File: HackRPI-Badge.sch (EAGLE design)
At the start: 42 parts, among them J1 FTDI_BASICPTH, J2 SOLDERJUMPERTRACE-PTH, U2 3.3V, U4 74595, U5 74595, U6 74595, U7 74165DT, U8 AT25FS010

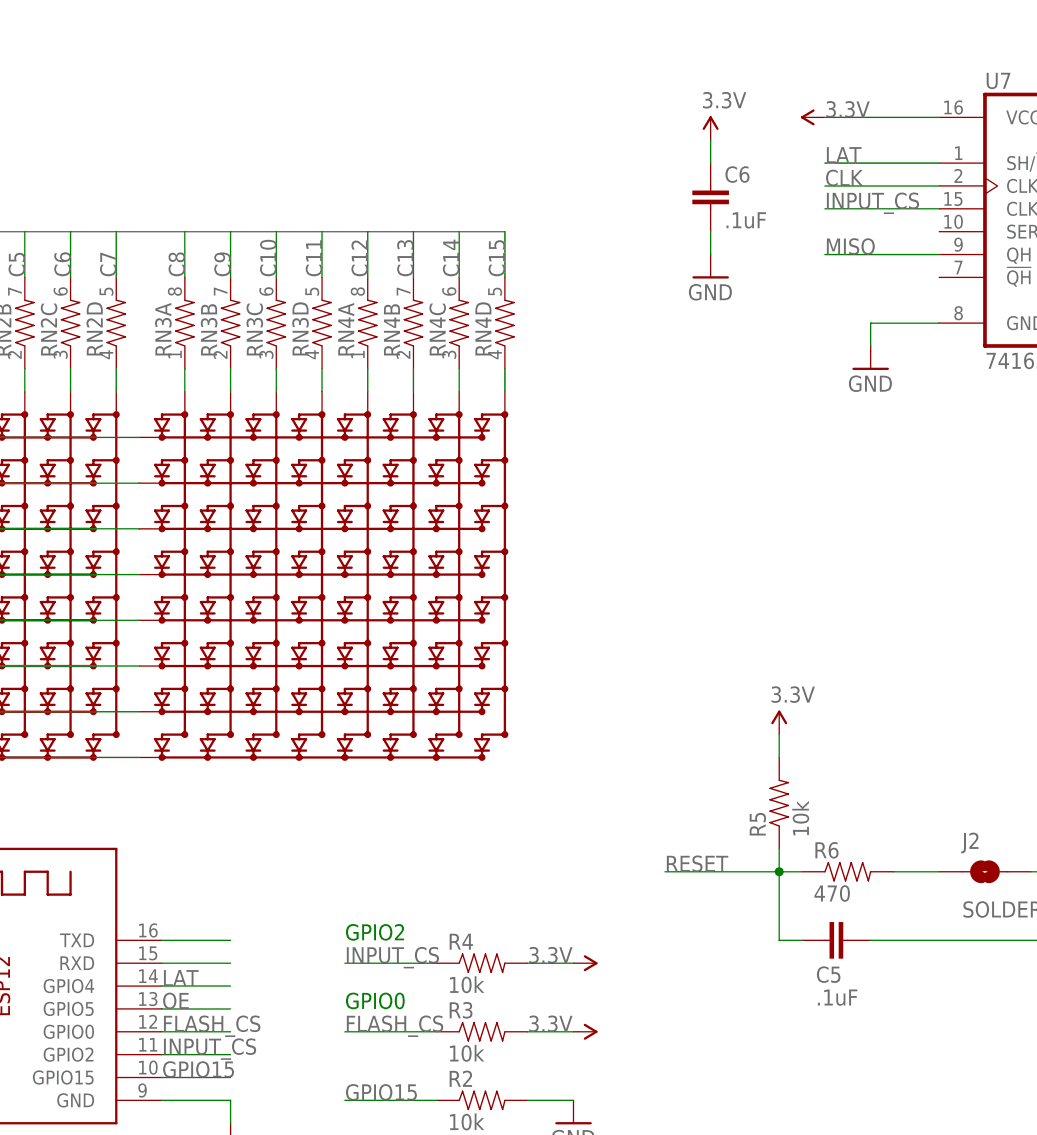
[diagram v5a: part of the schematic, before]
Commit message: Fixed 74165 sck pin connection, updated gitignore to ignore lock files
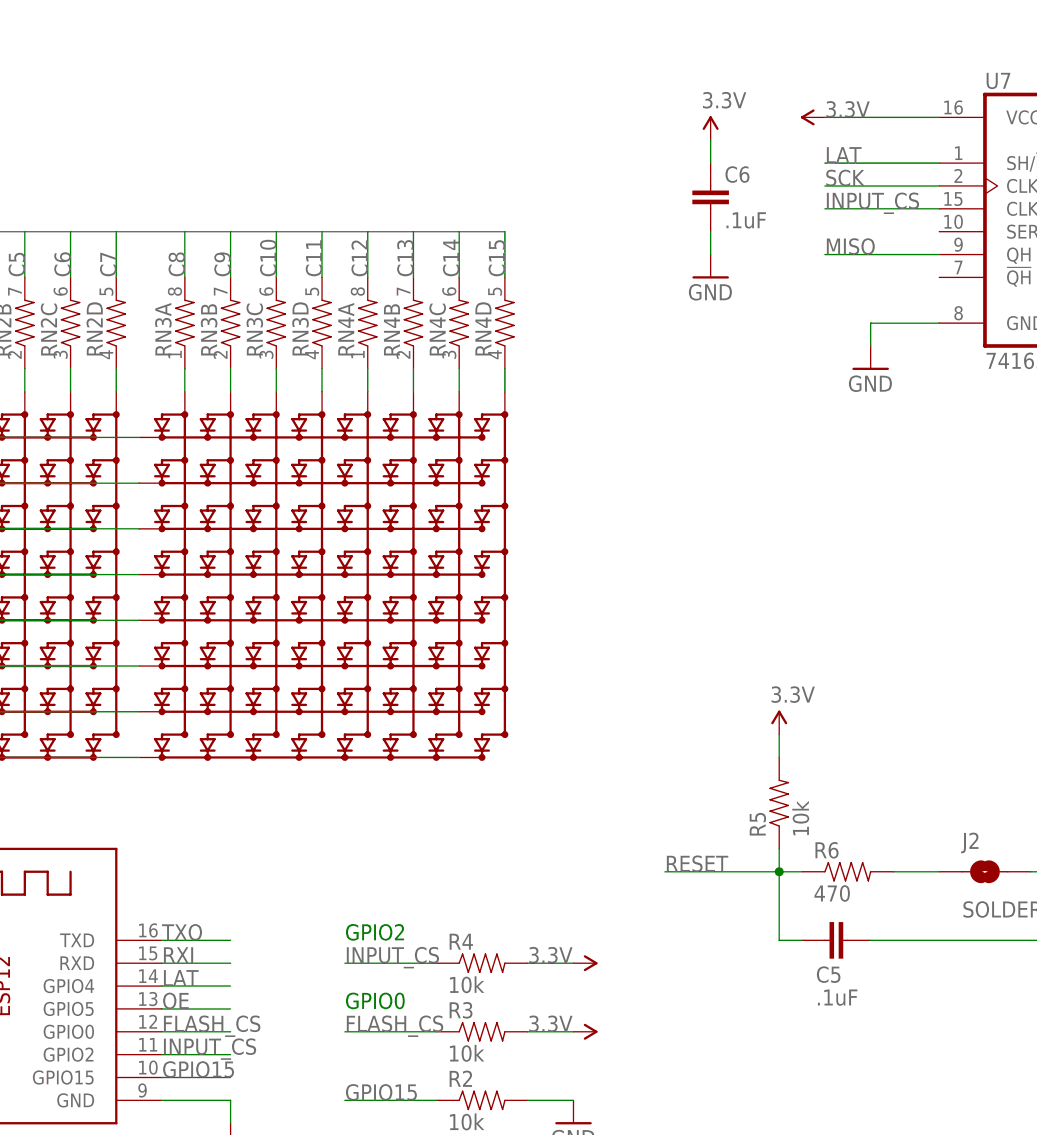
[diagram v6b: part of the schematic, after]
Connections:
- removed net CLK: U7.CLK
- net SCK: now also U7.CLK
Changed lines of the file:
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@@
 <pinref part="U8" gate="G$1" pin="SCK"/>
+</segment>
+<segment>
+<pinref part="U7" gate="A" pin="CLK"/>
+<wire x1="104.14" y1="88.9" x2="91.44" y2="88.9" width="0.1524" layer="91"/>
+<label x="91.44" y="88.9" size="1.778" layer="95"/>
 </segment>
 </net>
@@
 <pinref part="U1" gate="G$1" pin="TXD"/>
 <wire x1="17.78" y1="5.08" x2="25.4" y2="5.08" width="0.1524" layer="91"/>
+<label x="17.78" y="5.08" size="1.778" layer="95"/>
 </segment>
 <segment>
@@
 <pinref part="U1" gate="G$1" pin="RXD"/>
 <wire x1="17.78" y1="2.54" x2="25.4" y2="2.54" width="0.1524" layer="91"/>
+<label x="17.78" y="2.54" size="1.778" layer="95"/>
 </segment>
 <segment>
@@
 <wire x1="129.54" y1="86.36" x2="134.62" y2="86.36" width="0.1524" layer="91"/>
 <label x="129.54" y="86.36" size="1.778" layer="95"/>
-</segment>
-</net>
-<net name="CLK" class="0">
-<segment>
-<pinref part="U7" gate="A" pin="CLK"/>
-<wire x1="104.14" y1="88.9" x2="91.44" y2="88.9" width="0.1524" layer="91"/>
-<label x="91.44" y="88.9" size="1.778" layer="95"/>
 </segment>
 </net>
@@
 </sheet>
 </sheets>
+<errors>
+</errors>
 </schematic>
 </drawing>

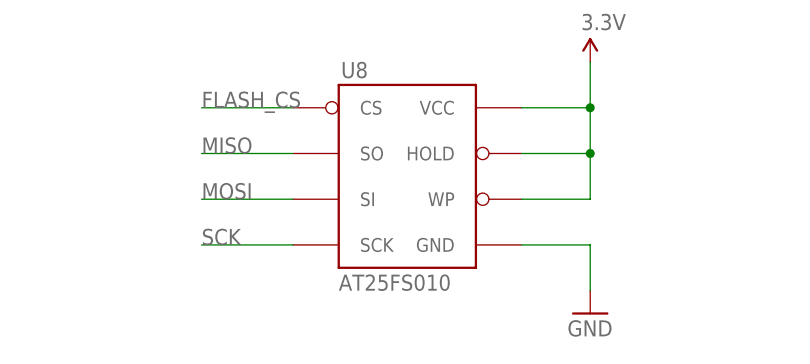
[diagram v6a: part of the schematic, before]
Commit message: Fixed bom part numbers
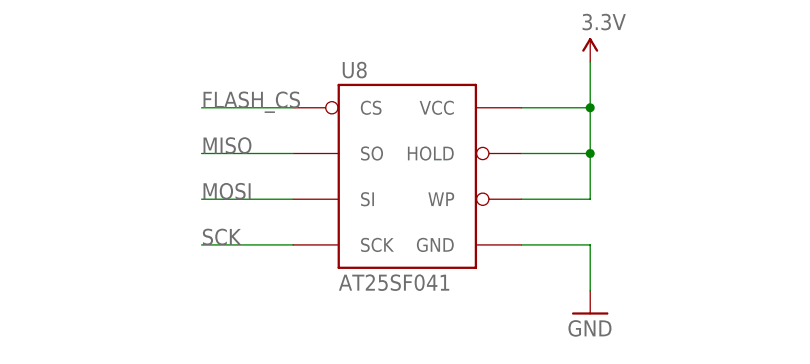
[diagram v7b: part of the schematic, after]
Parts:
- BAT1, BAT2: PARTNO (none) -> BK-82
- C1, C2, C3, C4, C5, C6, C7: PARTNO (none) -> CC0603ZRY5V9BB104
- C_IN, C_OUT: PARTNO (none) -> CL21A475KQFNNNG
- L1: PARTNO (none) -> CIG22L4R7MNE
- LED_LEFT, LEF_RIGHT: PARTNO (none) -> LDM-13488MI
- R1: PARTNO (none) -> RC0603JR-071ML
- R2, R3, R4, R5: PARTNO (none) -> RC0603JR-0710KL
- R6: PARTNO (none) -> RC0603JR-07470RL
- RN1, RN2, RN3, RN4: PARTNO (none) -> YC164-JR-0747RL
- RN5, RN6: PARTNO (none) -> 742C083103JP
- S1, S2, S3, S4, S5, S6: PARTNO (none) -> 1825910-6
- U1: PARTNO (none) -> 2491
- U2: PARTNO (none) -> AAT1217ICA-3.3-T1
- U3: PARTNO (none) -> ULN2803AFWG,C,EL
- U4, U5, U6: PARTNO (none) -> 74HC595PW,118
- U7: PARTNO (none) -> MC74HC165ADTR2G
- U8: value AT25FS010 -> AT25SF041; PARTNO (none) -> AT25SF041-SSHD-T
